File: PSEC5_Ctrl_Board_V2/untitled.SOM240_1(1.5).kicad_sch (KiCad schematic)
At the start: 24 parts, among them J10 ADM6-60-01.5-L-4-2-A-TR, J7 1766453, SW2 SW_MEC_5G

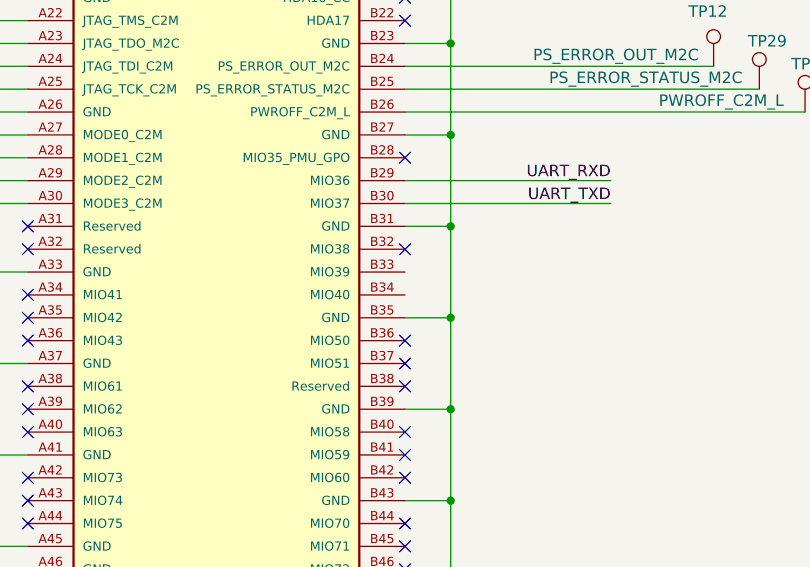
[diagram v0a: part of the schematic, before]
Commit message: Updated V2
New Power Planes, roruing of bottom samtec and kria positions
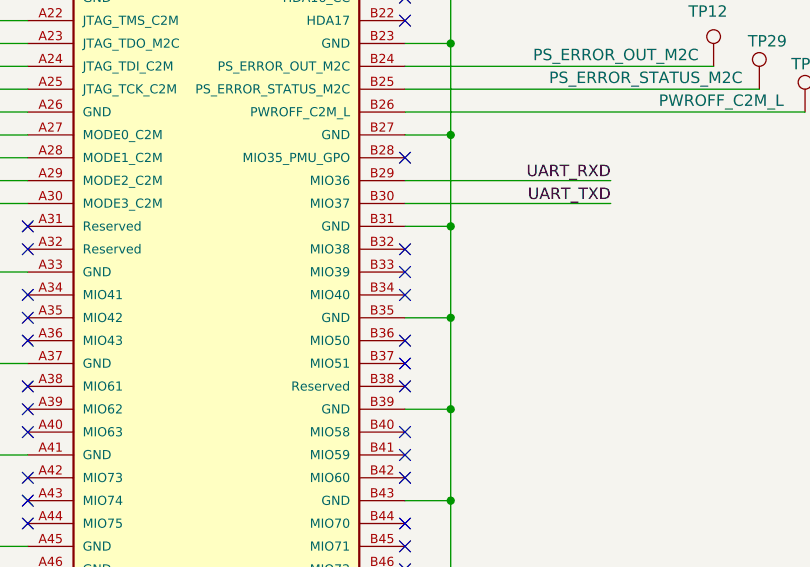
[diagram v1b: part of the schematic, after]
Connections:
- no-connect marks 59 -> 61

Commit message: Updated kria
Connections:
- net ETH_RXD0: now also J10.B45 (MIO71); no longer J10.C43 (MIO68)
- net ETH_RXD1: now also J10.B46 (MIO72); no longer J10.C42 (MIO67)
- net ETH_RXD2: now also J10.A42 (MIO73); no longer J10.C39 (MIO56)
- net ETH_RXD3: now also J10.A43 (MIO74); no longer J10.C38 (MIO55)
- net ETH_RX_CLK: now also J10.B44 (MIO70); no longer J10.C40 (MIO57)
- net ETH_RX_CTRL: now also J10.A44 (MIO75); no longer J10.C44 (MIO69)
- net ETH_TXD2: now also R3.1; no longer R3.2
- net ETH_TXD3: now also R7.1; no longer R7.2
- net ETH_TX_CTRL: now also R1.1; no longer R1.2
- net SD_CLK: now also J10.B37 (MIO51); no longer J10.D28 (MIO26)
- net SD_CMD: now also J10.B36 (MIO50); no longer J10.C34 (MIO47)
- net SD_DAT0: now also J10.D34 (MIO46); no longer J10.D30 (MIO28)
- net SD_DAT1: now also J10.C34 (MIO47); no longer J10.D29 (MIO27)
- net SD_DAT2: now also J10.C35 (MIO48); no longer J10.C36 (MIO49)
- net SD_DAT3: now also J10.C36 (MIO49); no longer J10.C35 (MIO48)
- net SD_DETECT_0: now also J10.B33 (MIO39); no longer J10.D34 (MIO46)
- net at R6.1: now also J10.D40 (MIO64); no longer J10.D41 (MIO65)
- net at J10.D42 (MIO66): now also R4.1; no longer R7.1
- net at J10.D37 (MIO53): no longer R3.1
- net at J10.D36 (MIO52): no longer R1.1
- net at R5.1: now also J10.D41 (MIO65); no longer J10.D40 (MIO64)
- net SD_PWR_EN: now reaches J10.A36 (MIO43)
- net at J10.D38 (MIO54): no longer R4.1
- new net: J10.C43 (MIO68), R7.2
- new net: J10.C42 (MIO67), R3.2
- new net: J10.C44 (MIO69), R1.2
- no-connect marks 61 -> 52
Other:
- note removed: "ETH_RGMI"
- moved on the sheet: R1, R3, R4, R5, R6, R7

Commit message: save Checkpoint, building out new SD
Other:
- added sheet SD_New (SD_New.kicad_sch)
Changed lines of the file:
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@@
+	)
+	(sheet
+		(at 355.6 200.66)
+		(size 38.1 20.32)
+		(exclude_from_sim no)
+		(in_bom yes)
+		(on_board yes)
+		(dnp no)
+		(fields_autoplaced yes)
+		(stroke
+			(width 0.1524)
+			(type solid)
+		)
+		(fill
+			(color 0 0 0 0.0000)
+		)
+		(property "Sheetname" "SD_New"
+			(at 355.6 199.9484 0)
+			(effects
+				(font
+					(size 1.27 1.27)
+				)
+				(justify left bottom)
+			)
+		)
+		(property "Sheetfile" "SD_New.kicad_sch"
+			(at 355.6 221.5646 0)
+			(effects
+				(font
+					(size 1.27 1.27)
+				)
+				(justify left top)
+			)
+		)
+		(instances
+			(project "PSEC5_Ctrl_Board"
+				(path "/165f2ae6-d522-4adf-a6c4-bb137b209d33/1f6d7a03-cfad-4370-8d2b-49ab19e248d8"
+					(page "14")
+				)
+			)
+		)
 	)
 	(sheet

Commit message: Updated Schematic with New SD implemented
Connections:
- net SD_DETECT_0 renamed SD_SEL
- net SD_DETECT_1 renamed SD_DETECT
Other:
- removed sheet SDcard1
- sheet SD_New ports: added SD_CLKA, SD_CMDA, SD_DAT0A, SD_DAT1A, SD_DAT2A, SD_DAT3A, SD_DETECT, SD_SEL; removed none

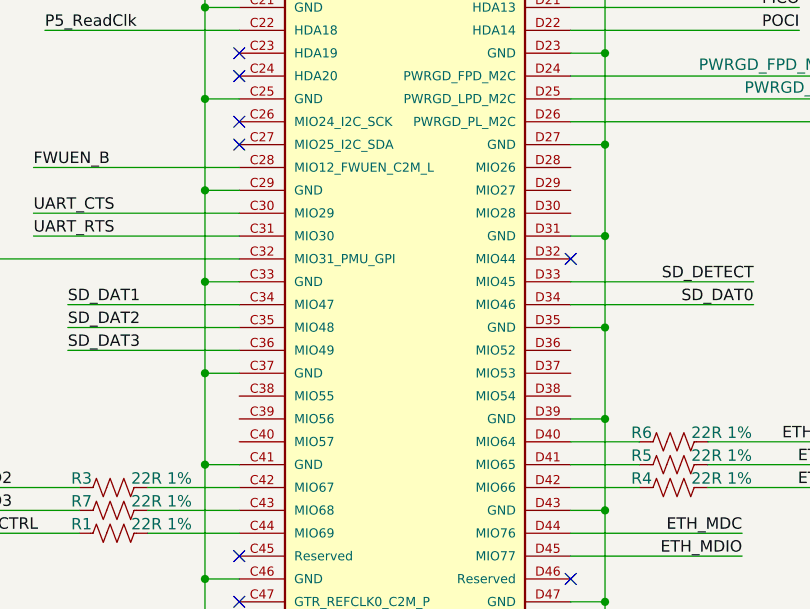
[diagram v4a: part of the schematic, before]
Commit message: fixed small ERC errors
Added no connection on open pins
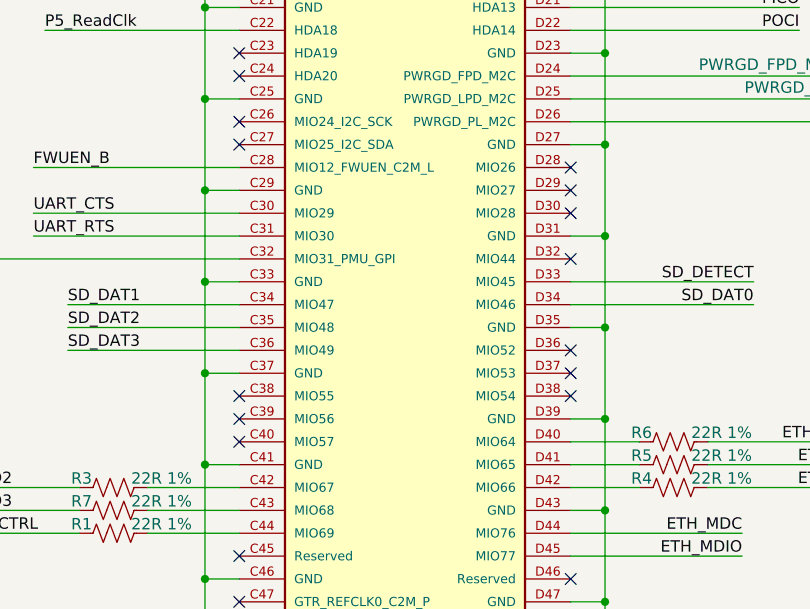
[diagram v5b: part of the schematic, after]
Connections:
- no-connect marks 52 -> 61
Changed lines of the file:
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@@
+	)
+	(no_connect
+		(at 214.63 121.92)
 	)
 	(no_connect
@@
 	)
 	(no_connect
+		(at 251.46 91.44)
+	)
+	(no_connect
 		(at 121.92 166.37)
 	)
@@
 	(no_connect
 		(at 214.63 160.02)
+	)
+	(no_connect
+		(at 251.46 114.3)
 	)
 	(no_connect
@@
 	)
 	(no_connect
+		(at 214.63 119.38)
+	)
+	(no_connect
+		(at 251.46 93.98)
+	)
+	(no_connect
 		(at 80.01 97.79)
 	)
@@
 	)
 	(no_connect
+		(at 214.63 116.84)
+	)
+	(no_connect
 		(at 121.92 90.17)
 	)
@@
 	(no_connect
 		(at 80.01 148.59)
+	)
+	(no_connect
+		(at 251.46 96.52)
 	)
 	(no_connect
@@
 	)
 	(no_connect
+		(at 251.46 116.84)
+	)
+	(no_connect
+		(at 251.46 111.76)
+	)
+	(no_connect
